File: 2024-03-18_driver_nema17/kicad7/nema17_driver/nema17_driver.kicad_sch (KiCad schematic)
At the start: 57 parts, among them Q1 8MHz n.m., U1 AS5600, U2 SP3485CN, U3 STM32C031C6T6, X1 IN, X2 OUT, X3 MOTOR, X4 JTAG, X5 DEBUG

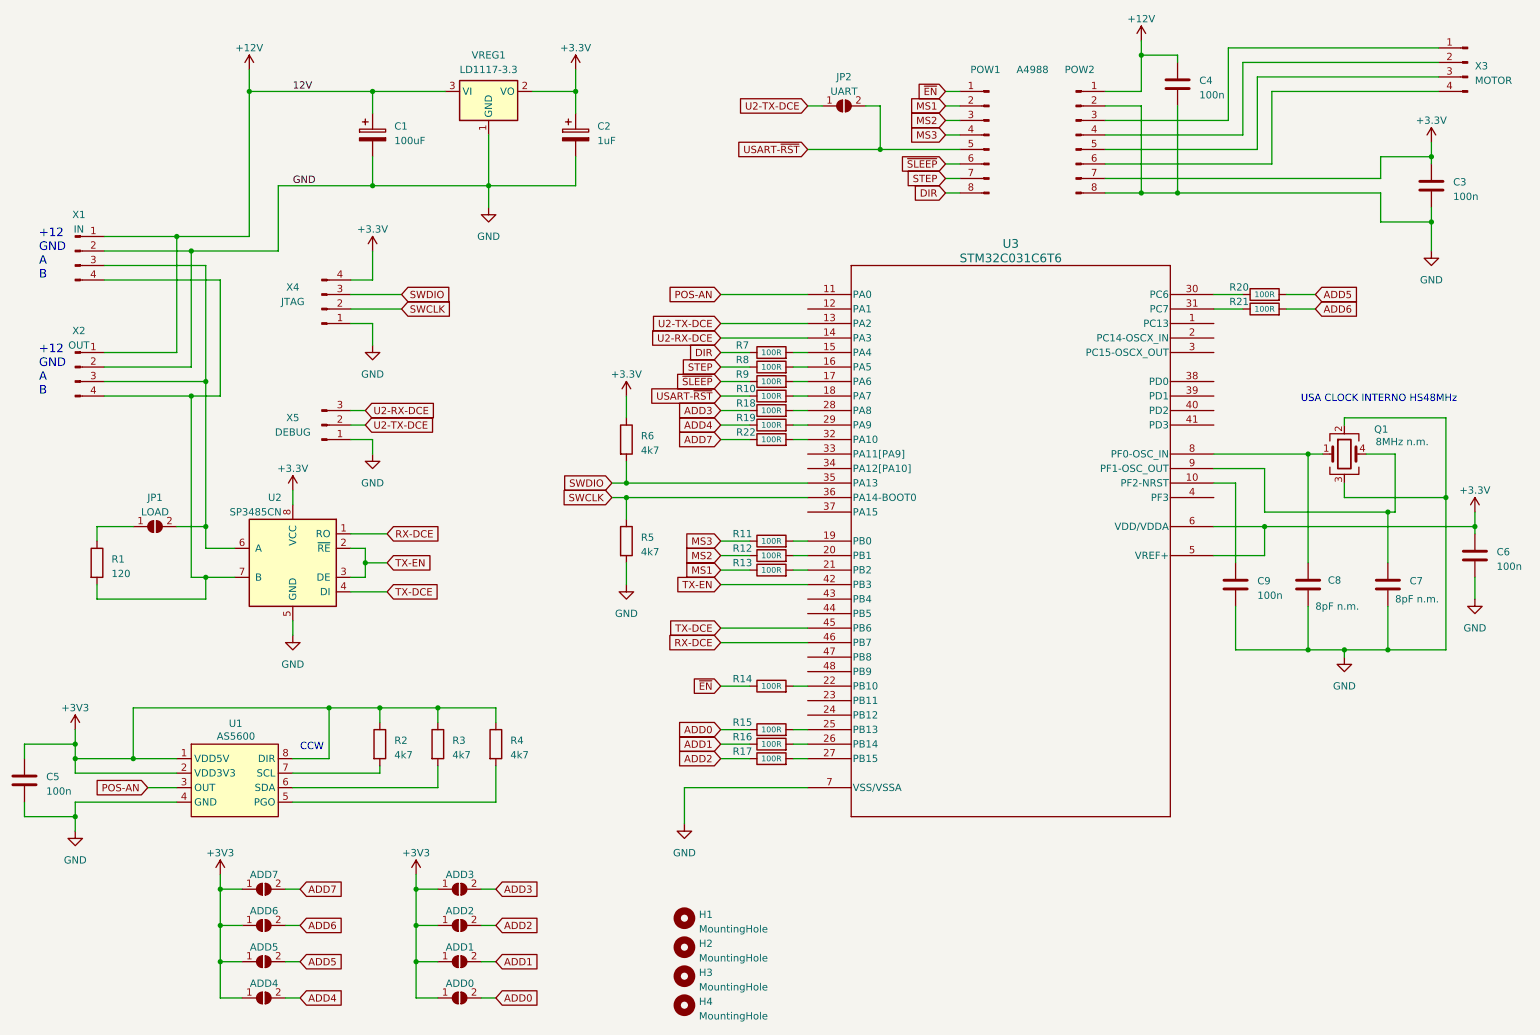
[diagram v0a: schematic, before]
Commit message: Posizionamento componenti
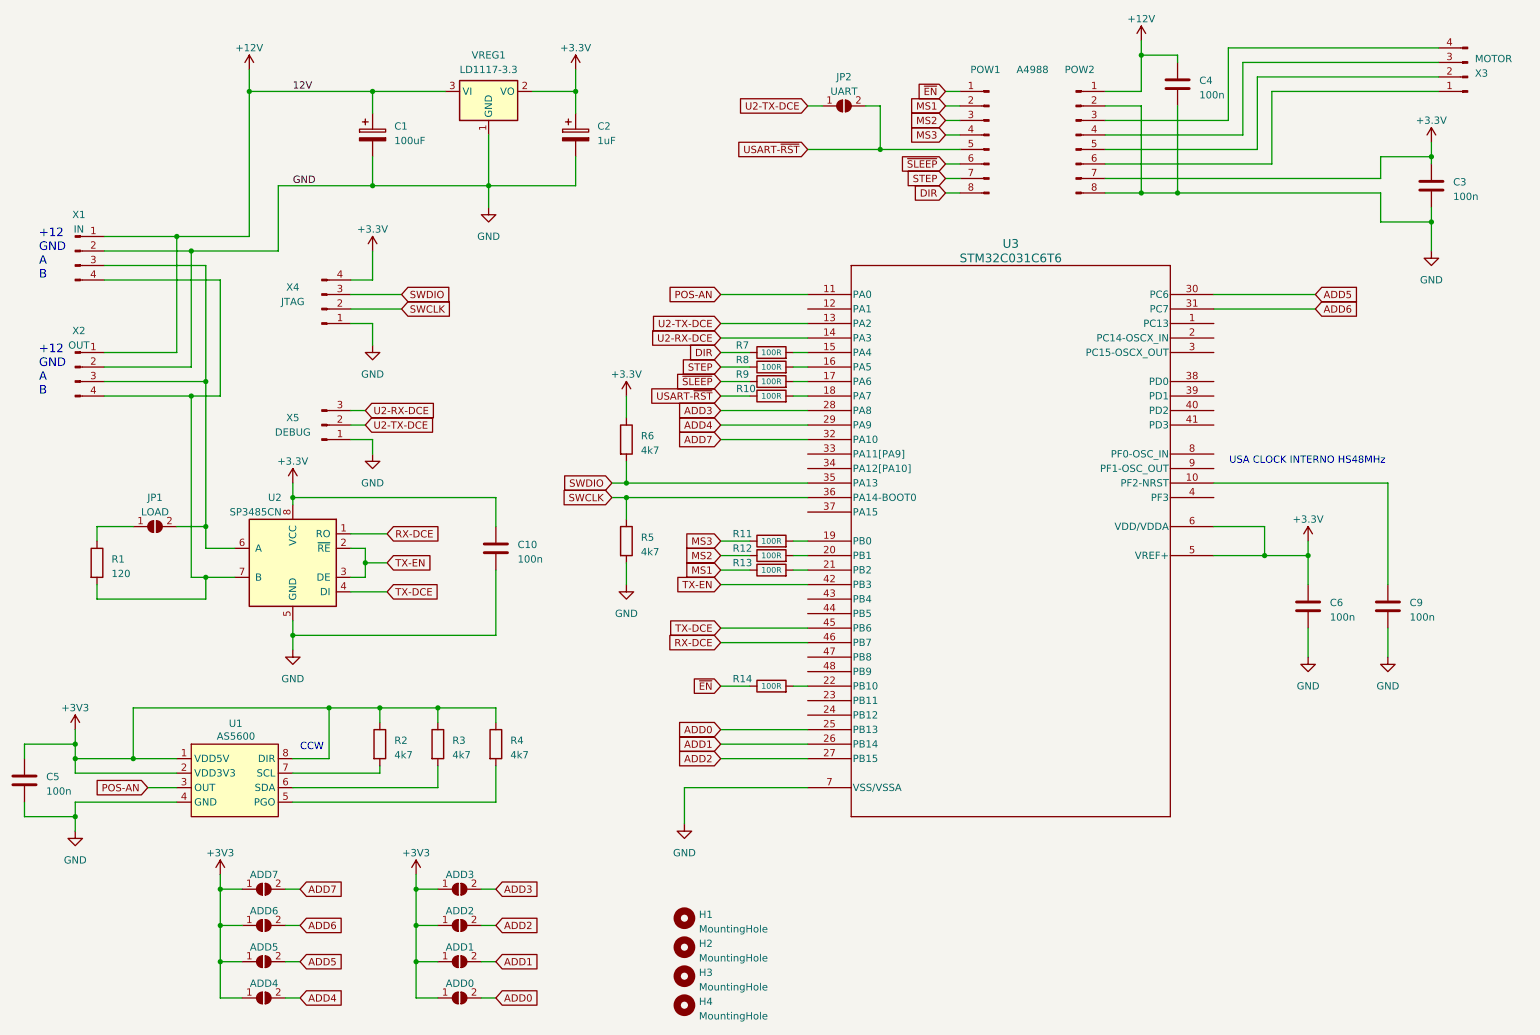
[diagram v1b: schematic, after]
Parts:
- removed C7, C8: 8pF n.m., Capacitor_SMD:C_0402_1005Metric, symbol Device:C
- removed Q1: 8MHz n.m., Crystal:Crystal_SMD_3225-4Pin_3.2x2.5mm, symbol Device:Crystal_GND23
- removed R15, R16, R17, R18, R19, R20, R21, R22: 100R, Resistor_SMD:R_0603_1608Metric, symbol Device:R
- added C10: 100n, Capacitor_SMD:C_0603_1608Metric, symbol Device:C
- X4: footprint Connector_PinSocket_2.54mm:PinSocket_1x04_P2.54mm_Vertical -> Connector_PinHeader_2.54mm:PinHeader_1x04_P2.54mm_Vertical
- X5: footprint Connector_PinSocket_2.54mm:PinSocket_1x03_P2.54mm_Vertical -> Connector_PinHeader_2.54mm:PinHeader_1x03_P2.54mm_Vertical
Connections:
- net +3.3V: now also C10.1
- net ADD0: now also U3.25 (PB13)
- net ADD1: now also U3.26 (PB14)
- net ADD2: now also U3.27 (PB15)
- net ADD3: now also U3.28 (PA8)
- net ADD4: now also U3.29 (PA9)
- net ADD5: now also U3.30 (PC6)
- net ADD6: now also U3.31 (PC7)
- net ADD7: now also U3.32 (PA10)
- net GND: now also C10.2
- net at POW2.3 (Pin_3): now also X3.4 (Pin_4); no longer X3.1 (Pin_1)
- net at POW2.4 (Pin_4): now also X3.3 (Pin_3); no longer X3.2 (Pin_2)
- net at POW2.5 (Pin_5): now also X3.2 (Pin_2); no longer X3.3 (Pin_3)
- net at POW2.6 (Pin_6): now also X3.1 (Pin_1); no longer X3.4 (Pin_4)
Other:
- moved on the sheet: C6, C9, X3

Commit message: Gerber
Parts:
- X1, X2: footprint Connector_PinSocket_2.54mm:PinSocket_1x04_P2.54mm_Vertical -> Connector_PinHeader_2.54mm:PinHeader_1x04_P2.54mm_Vertical
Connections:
- net +3V3 is gone; now on net +3.3V: C5.1, JP10.1 (A), JP3.1 (A), JP4.1 (A), JP5.1 (A), JP6.1 (A), JP7.1 (A), JP8.1 (A), JP9.1 (A), R2.1, R3.1, R4.1, U1.1 (VDD5V), U1.2 (VDD3V3), U1.8 (DIR)
- net at R7.2: now also U3.22 (PB10); no longer U3.15 (PA4)
- net at R8.2: now also U3.21 (PB2); no longer U3.16 (PA5)
- net at R13.2: now also U3.16 (PA5); no longer U3.21 (PB2)
- net at JP1.2 (B), U2.6 (A): now also X1.4 (Pin_4), X2.4 (Pin_4); no longer X1.3 (Pin_3), X2.3 (Pin_3)
- net at R1.2, U2.7 (B): now also X1.3 (Pin_3), X2.3 (Pin_3); no longer X1.4 (Pin_4), X2.4 (Pin_4)
- net at R11.2: now also U3.18 (PA7); no longer U3.19 (PB0)
- net at R14.2: now also U3.15 (PA4); no longer U3.22 (PB10)
- net at R10.2: now also U3.19 (PB0); no longer U3.18 (PA7)
- net at R12.2: now also U3.17 (PA6); no longer U3.20 (PB1)
- net at R9.2: now also U3.20 (PB1); no longer U3.17 (PA6)
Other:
- note added: "+12 GND B A"
- note added: "QUANDO SI USA IN MODALITÀ USART, CONFIGURARE COME GPIO-INPUT"
- note removed: "+12 GND A B"
- moved on the sheet: JP1, R1, R10, R11, R12, R13, R14, R5, R6, R7, R8, R9
